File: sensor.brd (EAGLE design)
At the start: 24 x 24 mm, 16 parts

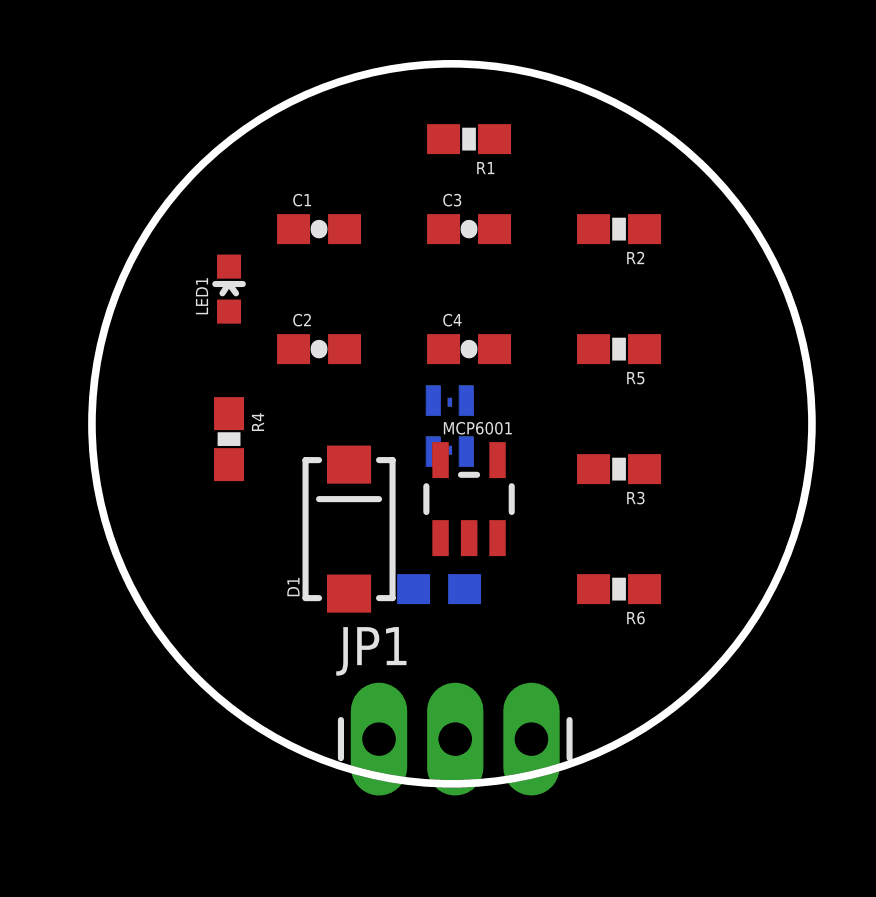
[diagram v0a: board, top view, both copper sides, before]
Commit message: sensor: pcb route completed
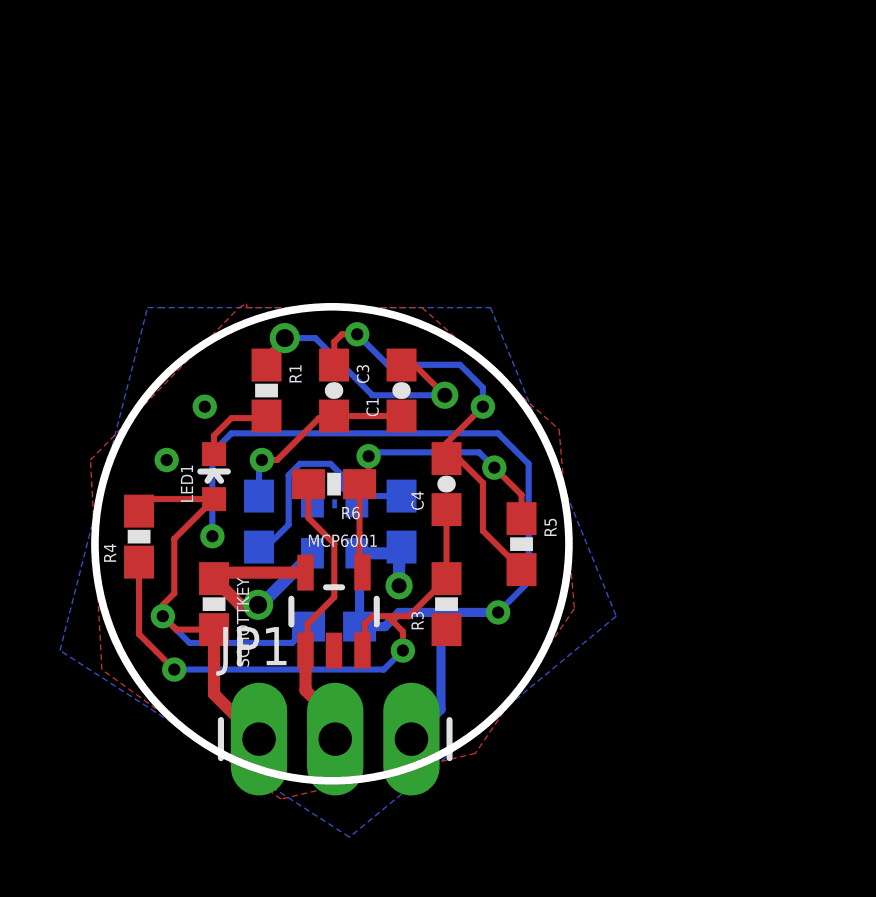
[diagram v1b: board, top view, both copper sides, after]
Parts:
- removed D1: (no value), SparkFun-DiscreteSemi:SMA-DIODE
- added SCHOTTKEY: 0, SparkFun-Resistors:0603-RES
- APDS1: device mylib:MINIATURE-CHIPLED -> librae:MINIATURE-CHIPLED
- moved R2 12.2 mm to (10.8, 9.25), flipped to the bottom, turned to 90 degrees
- moved R1 10.8 mm to (6.25, 13.6), turned to 270 degrees
- moved R6 10.1 mm to (8.50, 10.5)
- moved R3 7.30 mm to (12.2, 6.50), turned to 90 degrees
- moved R5 7.27 mm to (14.8, 8.50), turned to 270 degrees
- moved C3 7.01 mm to (8.50, 13.6), turned to 270 degrees
- moved LED1 6.27 mm to (4.50, 10.8)
- moved C2 6.09 mm to (6.00, 9.25), flipped to the bottom, turned to 270 degrees
- moved C1 6.04 mm to (10.8, 13.6), turned to 90 degrees
- moved MCP6001 5.86 mm to (8.50, 6.25)
- moved APDS1 5.64 mm to (8.50, 9.00)
- moved C4 4.56 mm to (12.2, 10.5), turned to 90 degrees
- moved R4 4.42 mm to (2.00, 8.75), turned to 90 degrees
- moved JP1 4.00 mm to (6.00, 2.00)
- moved C5 3.72 mm to (8.50, 5.75)
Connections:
- net VCC: now also SCHOTTKEY.2; no longer D1.A
- net VDD: now also SCHOTTKEY.1; no longer D1.C
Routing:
- net GND: track 0.00 -> 43.3 mm, vias 0 -> 7
- net N$10: track 0.00 -> 19.9 mm, vias 0 -> 2
- net VCC: track 0.00 -> 18.9 mm, vias 0 -> 1
- net N$9: track 0.00 -> 14.4 mm, vias 0 -> 2
- net N$6: track 0.00 -> 10.6 mm, vias 0 -> 2
- net OUT: track 0.00 -> 9.66 mm
- net N$7: track 0.00 -> 7.72 mm
- net VDD: track 0.00 -> 7.48 mm, vias 0 -> 1
- net N$8: track 0.00 -> 6.50 mm, vias 0 -> 1
- net N$3: track 0.00 -> 3.03 mm
- added copper zone on layer 1, net GND
- added copper zone on layer 16, net GND
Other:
- board size 24 x 24 mm -> 15.8 x 15.8 mm
